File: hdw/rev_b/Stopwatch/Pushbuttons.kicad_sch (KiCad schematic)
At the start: 42 parts, among them SW601 Cap_Touch, SW602 Cap_Touch, SW603 Cap_Touch, U601 AT42QT1010-TSHR, U602 AT42QT1010-TSHR, U603 AT42QT1010-TSHR, U604 74LVC1G97, U605 74LVC1G97, U606 74LVC1G97, U607 74LVC1G80, U608 74LVC1G80

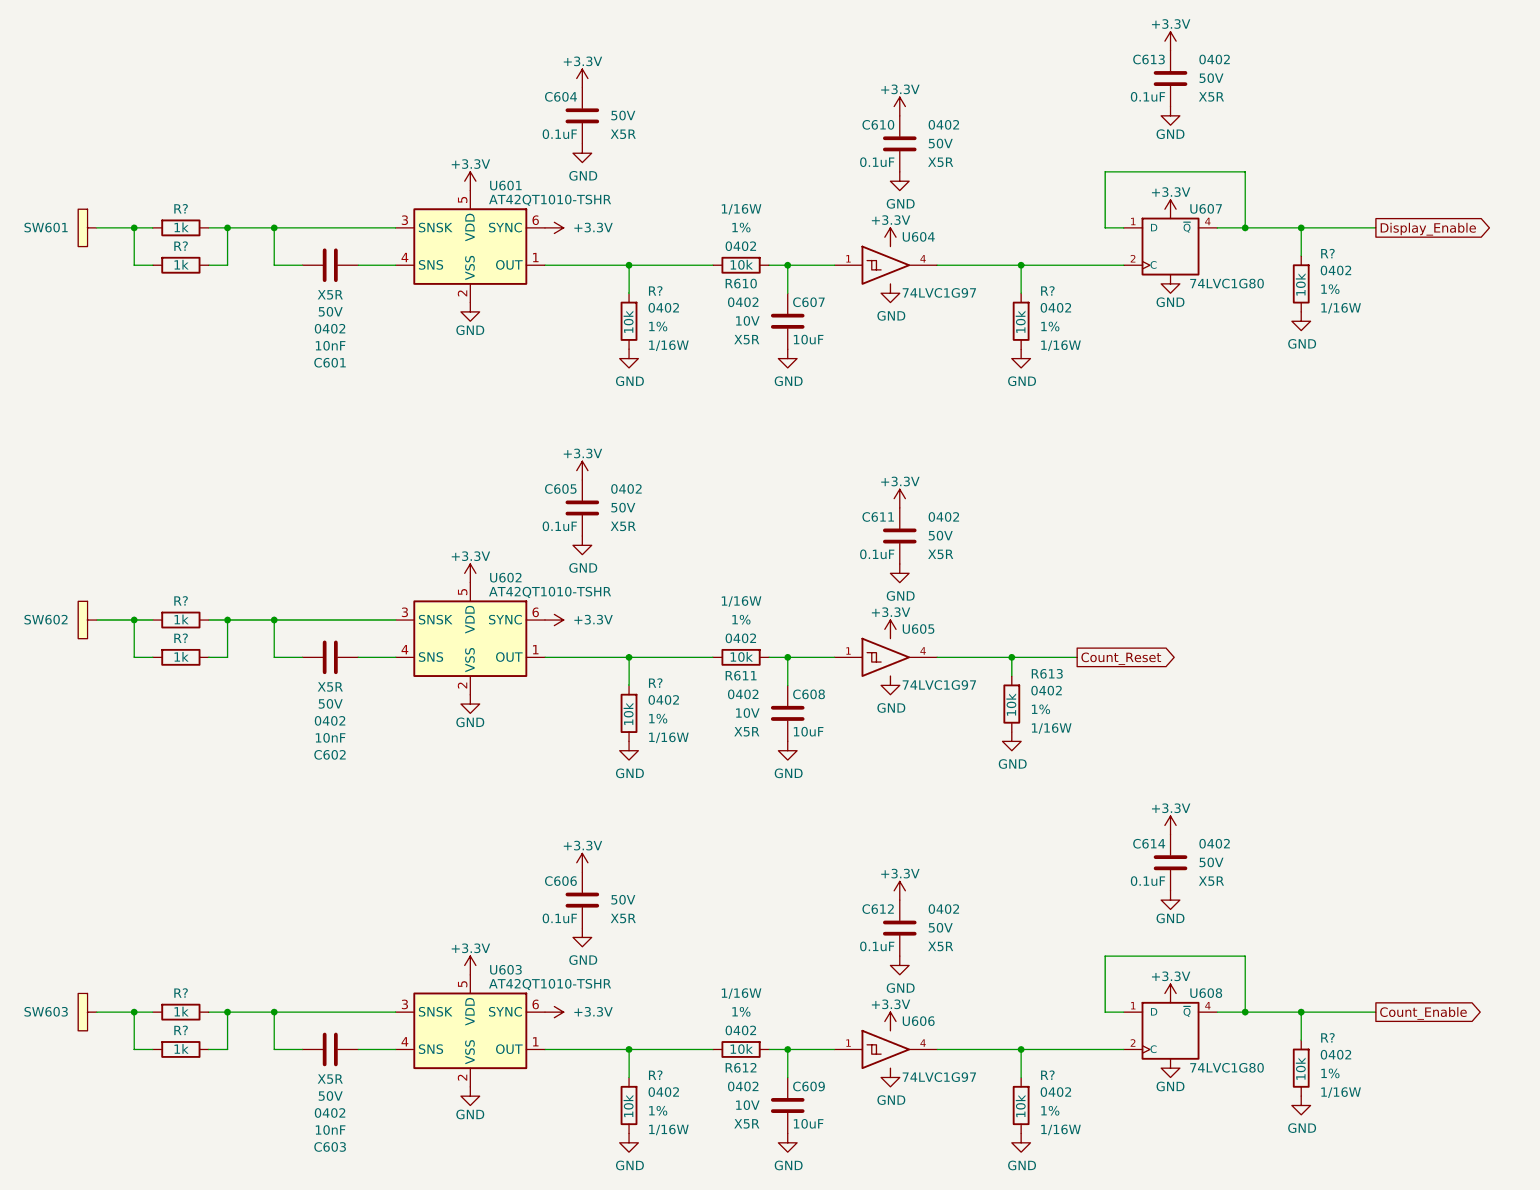
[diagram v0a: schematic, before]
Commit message: ported rev b to kicad 8
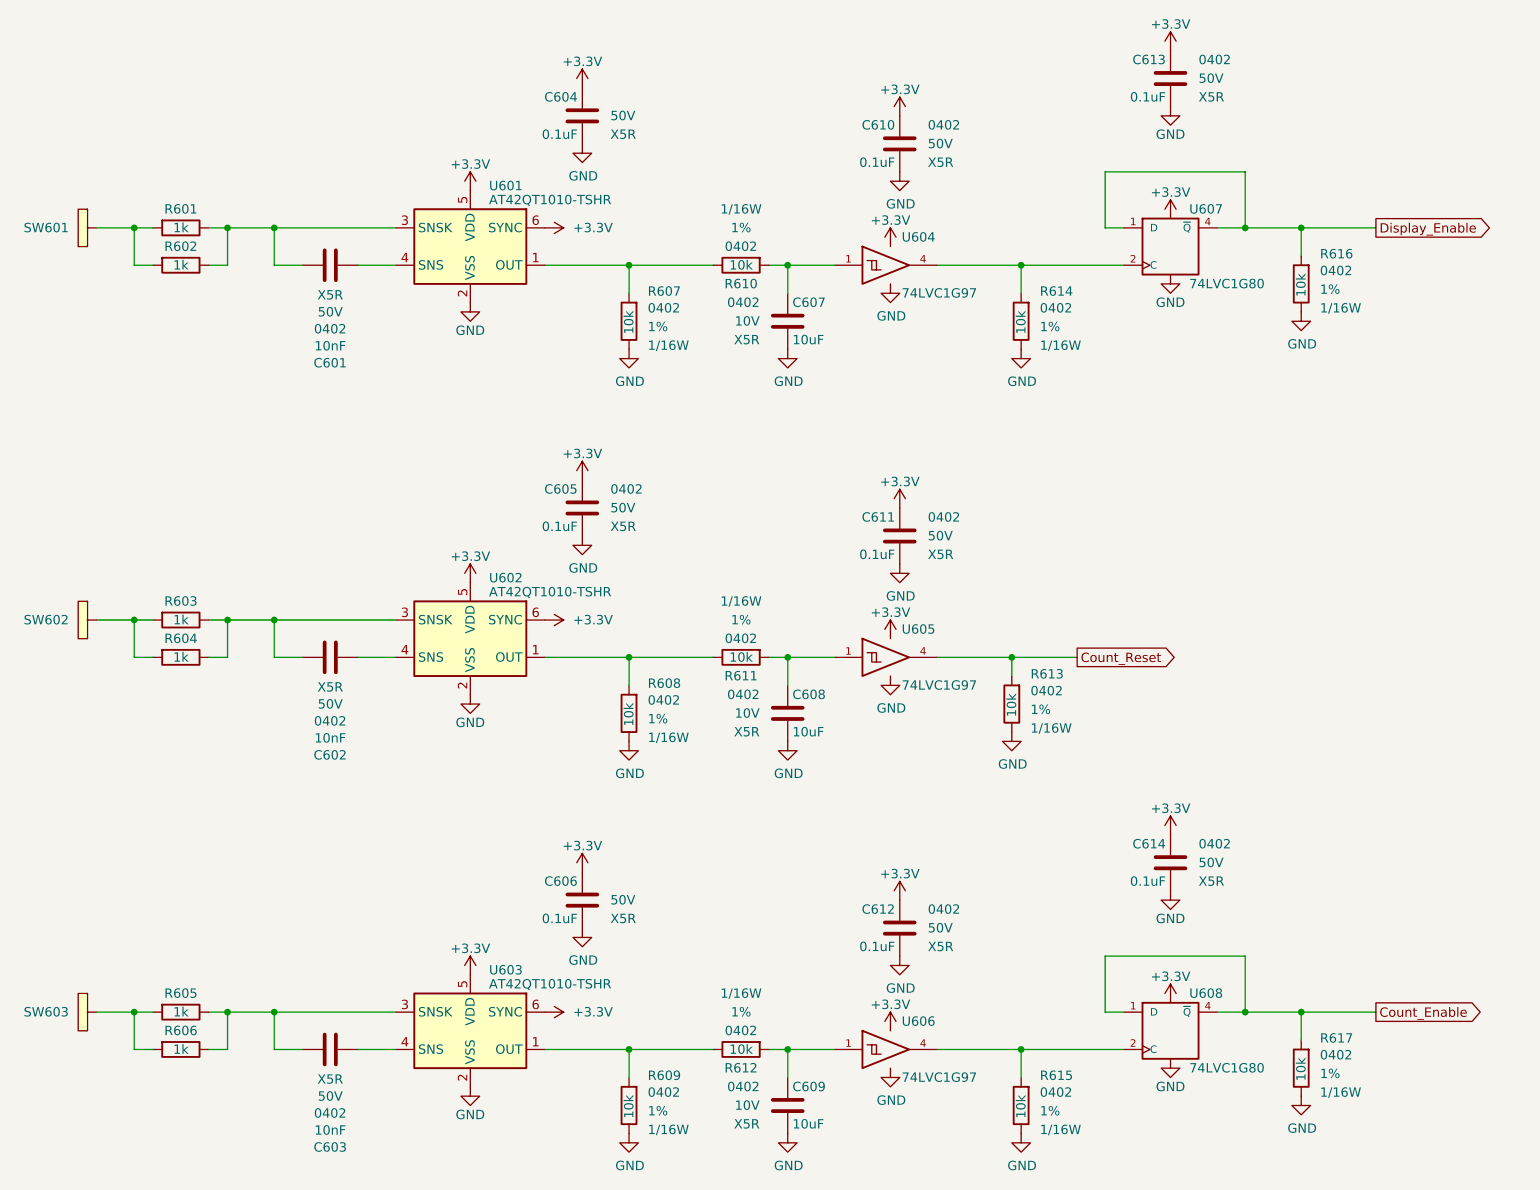
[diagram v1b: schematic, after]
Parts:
- gave numbers to parts that had none: 13

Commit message: integrated SC70 gates
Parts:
- U604, U605, U606: footprint Package_SON:Fairchild_MicroPak2-6_1.0x1.0mm_P0.35mm -> Package_TO_SOT_SMD:SOT-363_SC-70-6; Digi-Key PN 296-29875-1-ND -> 296-15582-1-ND
- U607, U608: footprint Package_SON:Texas_X2SON-5_0.8x0.8mm_P0.48mm -> Package_TO_SOT_SMD:SOT-353_SC-70-5; Digi-Key PN 1727-74LVC1G80GX,125CT-ND -> 296-41824-1-ND
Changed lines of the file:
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@@
 			)
 		)
-		(property "Footprint" "Package_SON:Texas_X2SON-5_0.8x0.8mm_P0.48mm"
+		(property "Footprint" "Package_TO_SOT_SMD:SOT-353_SC-70-5"
 			(at 194.31 44.45 0)
 			(effects
@@
 			)
 		)
-		(property "Digi-Key PN" "1727-74LVC1G80GX,125CT-ND"
+		(property "Digi-Key PN" "296-41824-1-ND"
 			(at 194.31 44.45 0)
 			(effects
@@
 			)
 		)
-		(property "Footprint" "Package_SON:Texas_X2SON-5_0.8x0.8mm_P0.48mm"
+		(property "Footprint" "Package_TO_SOT_SMD:SOT-353_SC-70-5"
 			(at 194.31 151.13 0)
 			(effects
@@
 			)
 		)
-		(property "Digi-Key PN" "1727-74LVC1G80GX,125CT-ND"
+		(property "Digi-Key PN" "296-41824-1-ND"
 			(at 194.31 151.13 0)
 			(effects
@@
 			)
 		)
-		(property "Footprint" "Package_SON:Fairchild_MicroPak2-6_1.0x1.0mm_P0.35mm"
+		(property "Footprint" "Package_TO_SOT_SMD:SOT-363_SC-70-6"
 			(at 157.48 153.67 0)
 			(effects
@@
 			)
 		)
-		(property "Digi-Key PN" "296-29875-1-ND"
+		(property "Digi-Key PN" "296-15582-1-ND"
 			(at 156.21 153.67 0)
 			(effects
@@
 			)
 		)
-		(property "Footprint" "Package_SON:Fairchild_MicroPak2-6_1.0x1.0mm_P0.35mm"
+		(property "Footprint" "Package_TO_SOT_SMD:SOT-363_SC-70-6"
 			(at 157.48 46.99 0)
 			(effects
@@
 			)
 		)
-		(property "Digi-Key PN" "296-29875-1-ND"
+		(property "Digi-Key PN" "296-15582-1-ND"
 			(at 156.21 46.99 0)
 			(effects
@@
 			)
 		)
-		(property "Footprint" "Package_SON:Fairchild_MicroPak2-6_1.0x1.0mm_P0.35mm"
+		(property "Footprint" "Package_TO_SOT_SMD:SOT-363_SC-70-6"
 			(at 157.48 100.33 0)
 			(effects
@@
 			)
 		)
-		(property "Digi-Key PN" "296-29875-1-ND"
+		(property "Digi-Key PN" "296-15582-1-ND"
 			(at 156.21 100.33 0)
 			(effects
